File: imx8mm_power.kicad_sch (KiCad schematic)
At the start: 58 parts, among them U1 MIMX8MM6DVTLZAA

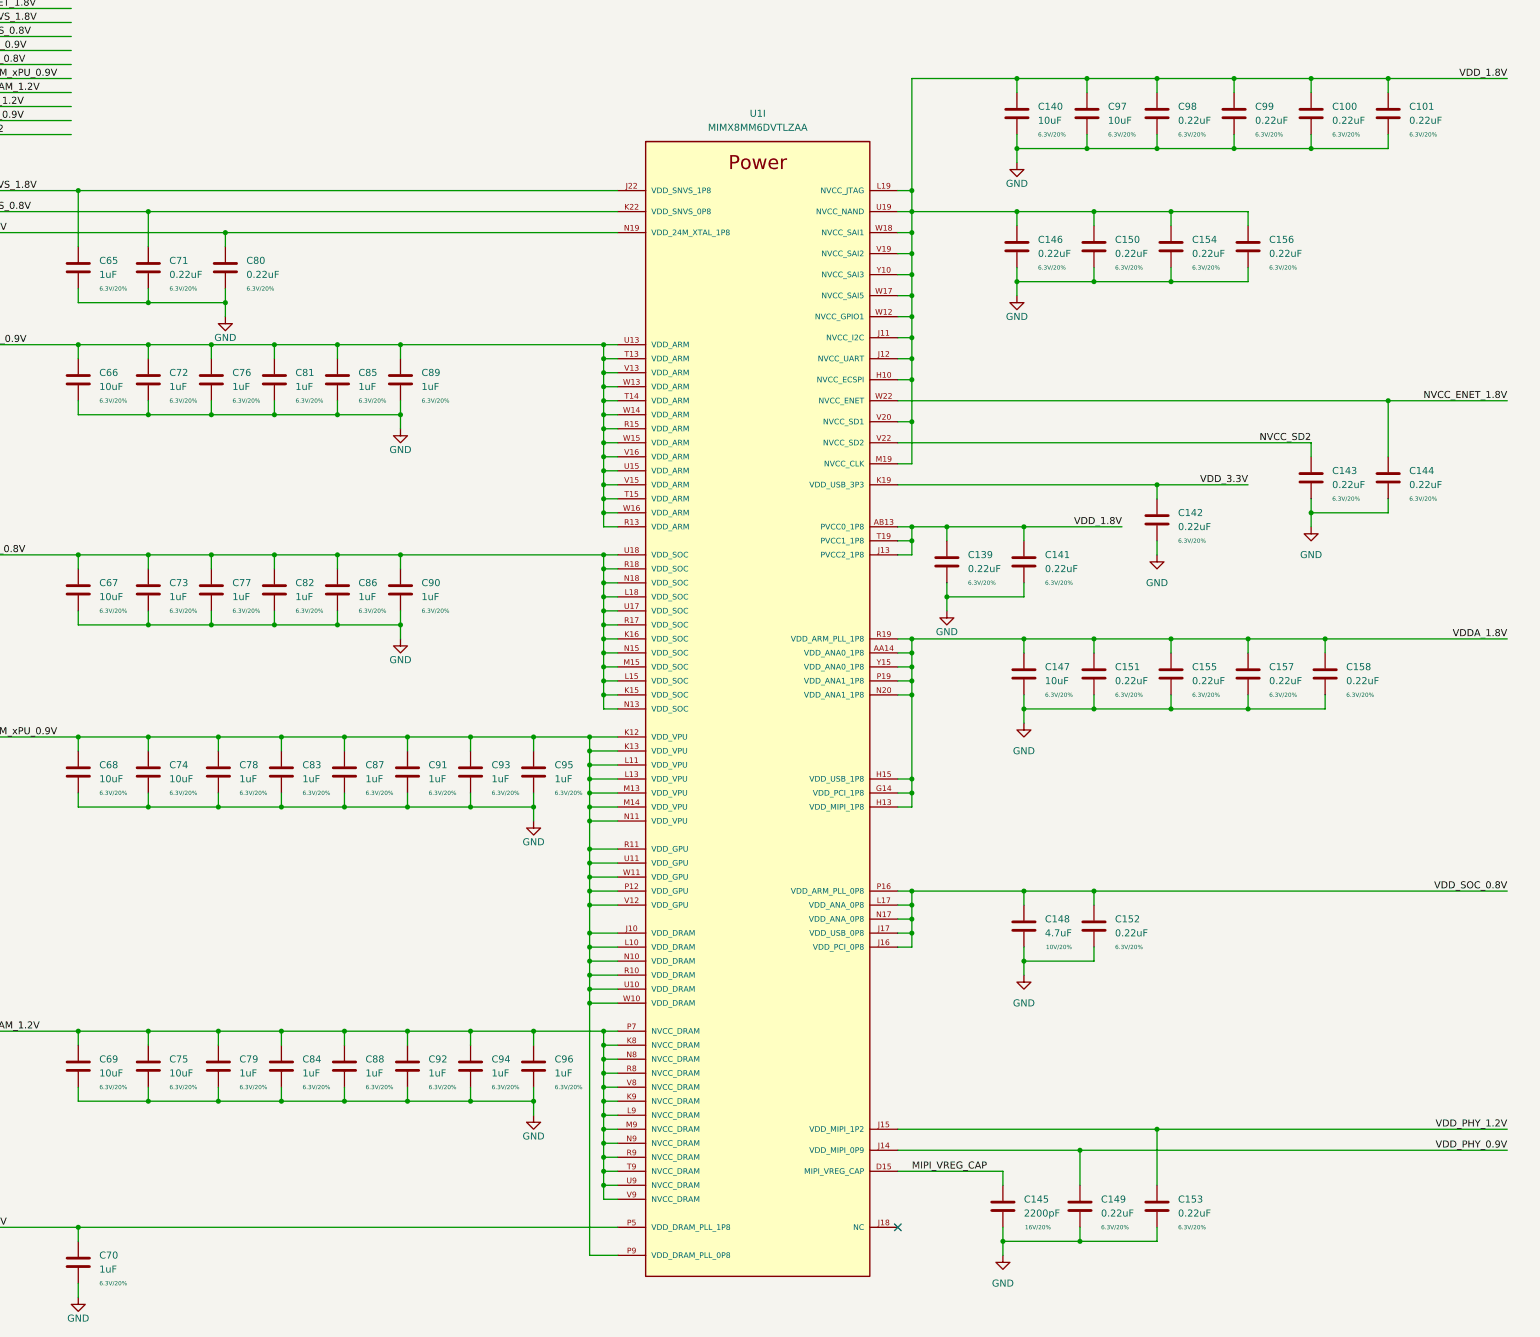
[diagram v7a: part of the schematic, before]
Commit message: fix ref desgigators, add table for dram config
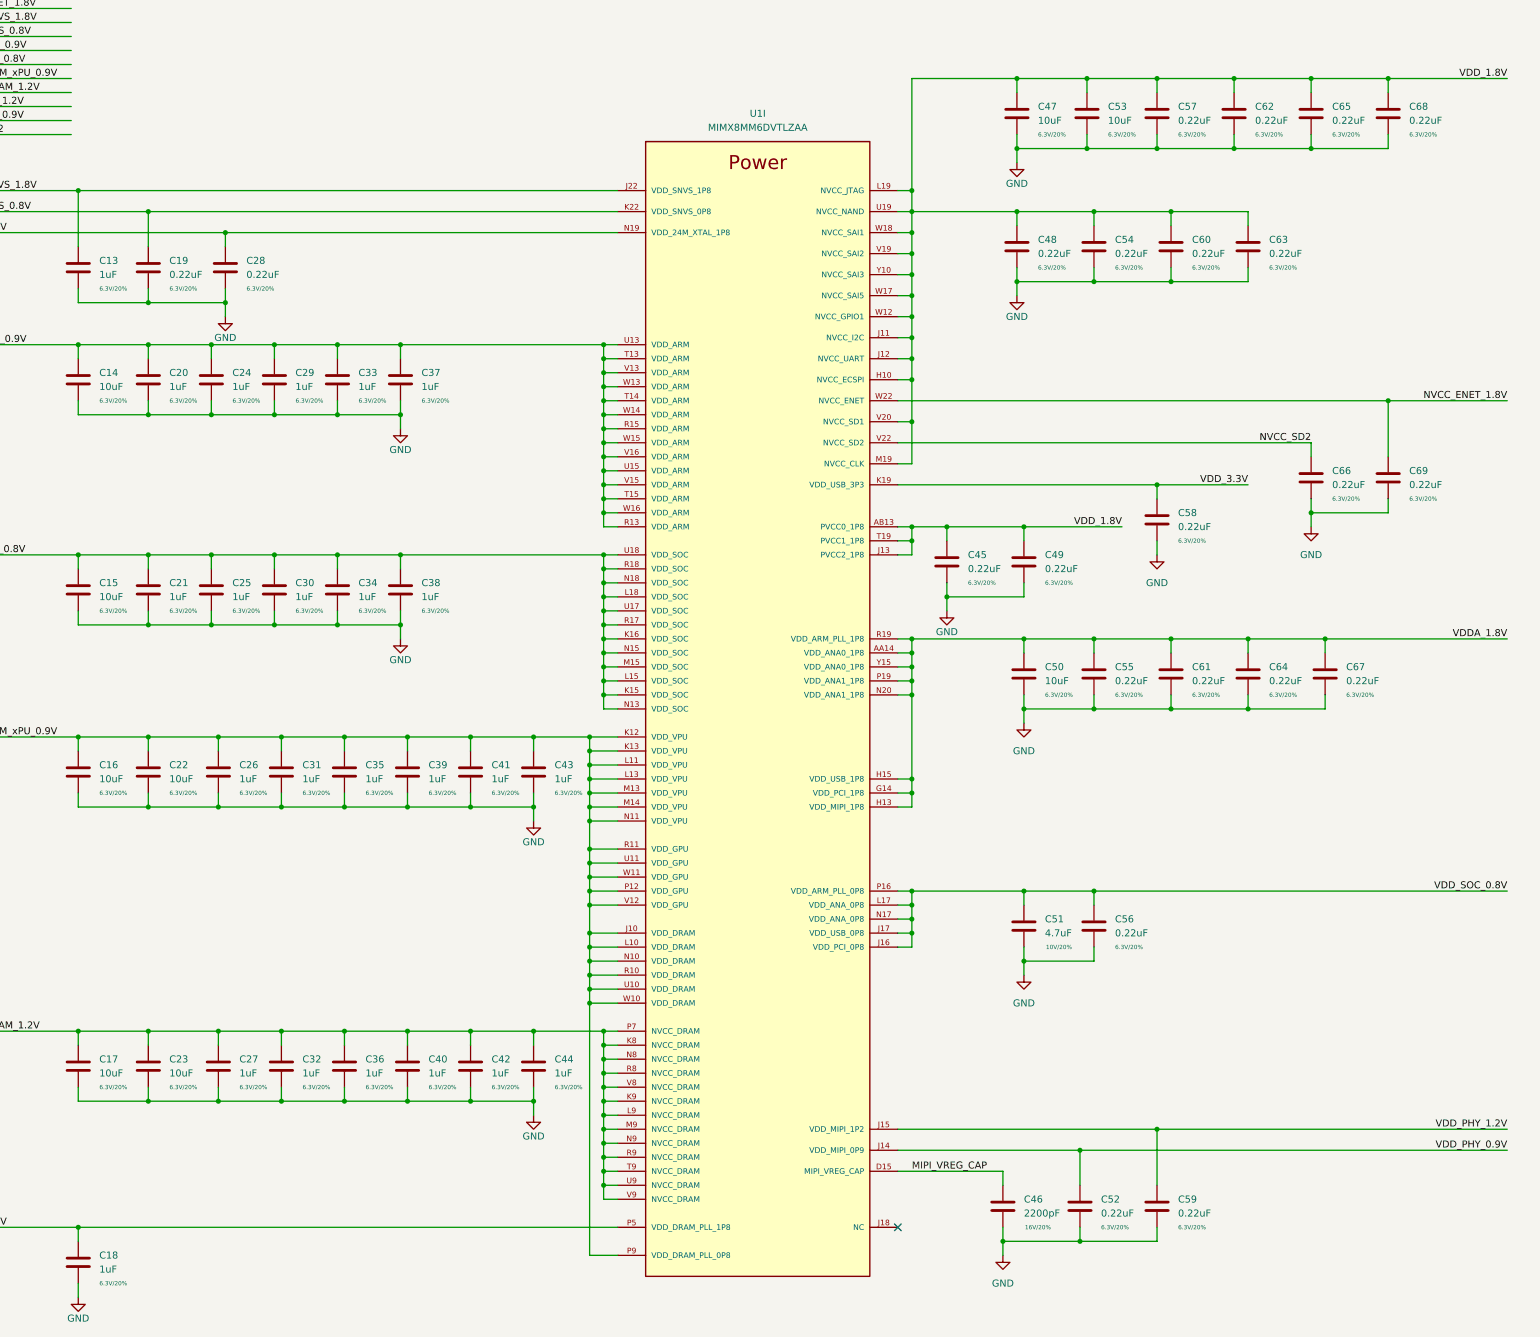
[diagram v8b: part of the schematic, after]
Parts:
- renumbered C65 to C13, C66 to C14, C67 to C15, C68 to C16, C69 to C17, C70 to C18, C71 to C19, C72 to C20, C73 to C21, C74 to C22, C75 to C23, C76 to C24, C77 to C25, C78 to C26, C79 to C27, C80 to C28, C81 to C29, C82 to C30, C83 to C31, C84 to C32, C85 to C33, C86 to C34, C87 to C35, C88 to C36, C89 to C37, C90 to C38, C91 to C39, C92 to C40, C93 to C41, C94 to C42, C95 to C43, C96 to C44, C139 to C45, C145 to C46, C140 to C47, C146 to C48, C141 to C49, C147 to C50, C148 to C51, C149 to C52, C97 to C53, C150 to C54, C151 to C55, C152 to C56, C98 to C57, C142 to C58, C153 to C59, C154 to C60, C155 to C61, C99 to C62, C156 to C63, C157 to C64, C100 to C65, C143 to C66, C158 to C67, C101 to C68, C144 to C69
